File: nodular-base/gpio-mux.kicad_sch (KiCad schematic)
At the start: 6 parts, among them U24 AW9523B, U25 AW9523B, U26 AW9523B

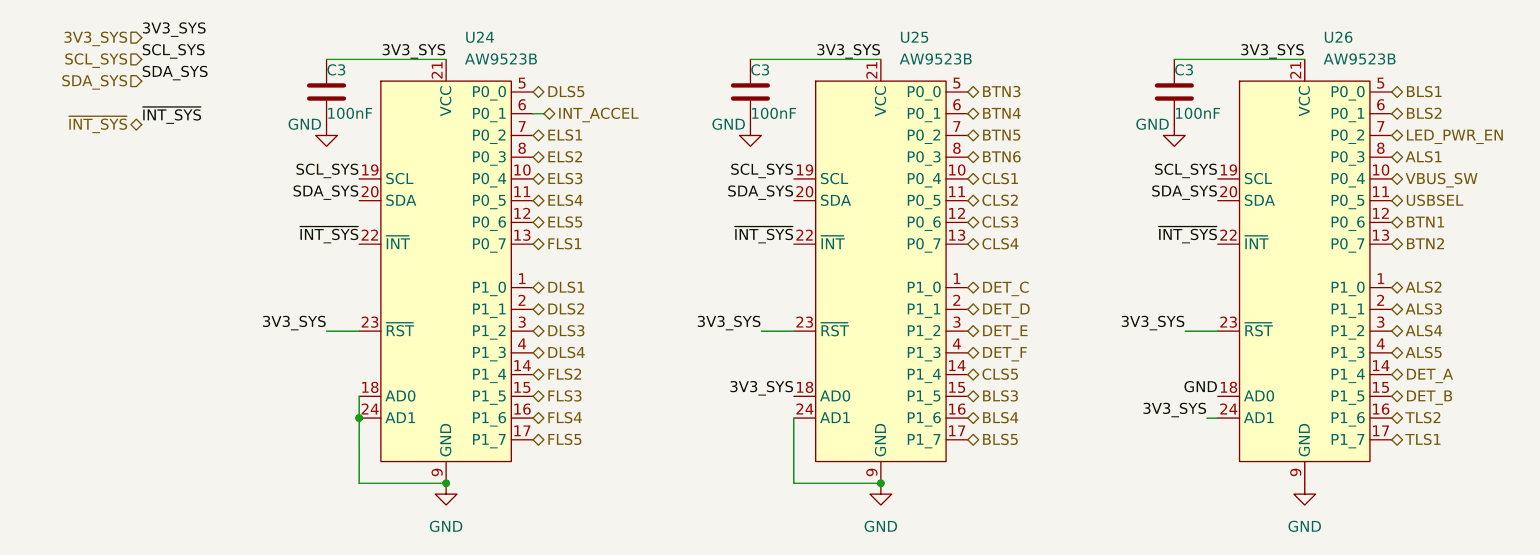
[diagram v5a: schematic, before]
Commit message: Modify base board: - Fix ESP32 strapping pins state - Remove 3/6 M3 standoffs - Change to LGA-style pads on ESP32 - Modify SFP mechanical pads to not be plated - Add larger mechanical pads with more solder paste surface to USB-C connectors
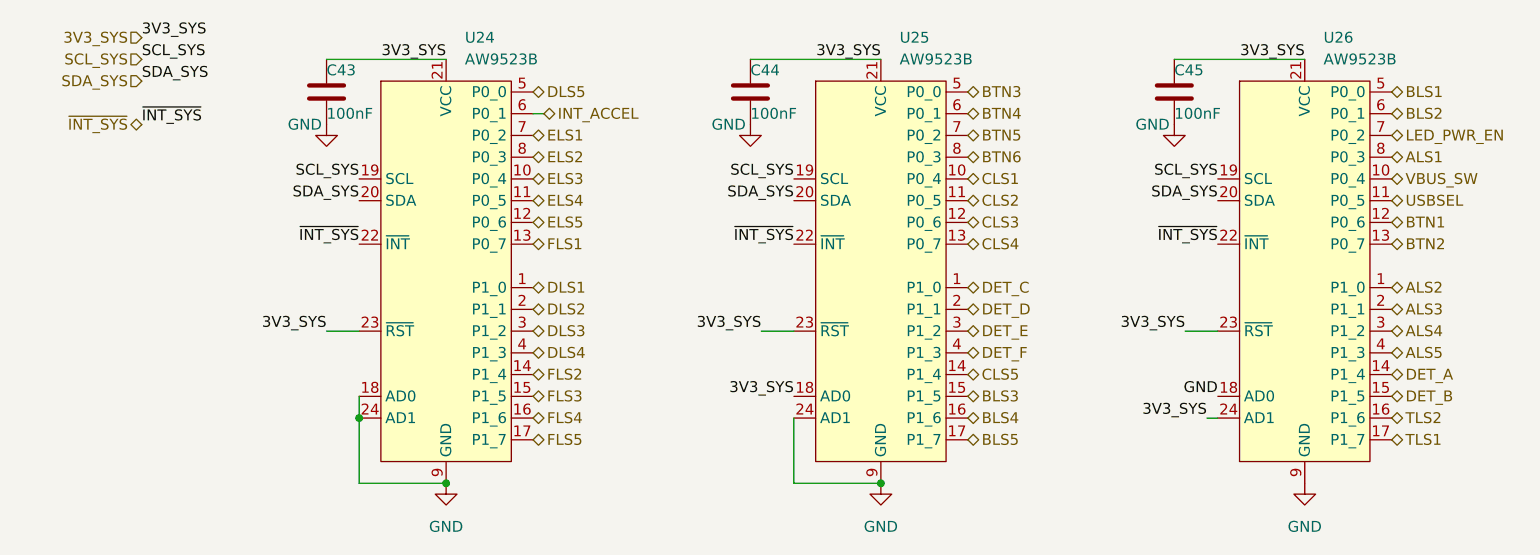
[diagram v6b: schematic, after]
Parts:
- renumbered C3 to C43, C3 to C44, C3 to C45
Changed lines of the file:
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@@
   (symbol (lib_id "Device:C") (at 180.34 64.77 0) (unit 1)
     (in_bom yes) (on_board yes) (dnp no)
-    (property "Reference" "C3" (at 180.34 62.23 0)
+    (property "Reference" "C45" (at 180.34 62.23 0)
       (effects (font (size 1.27 1.27)) (justify left))
     )
@@
     (instances
       (project "nodular-base"
-        (path "/6dcb0502-87e2-4c28-9ce8-81aab8925f06"
-          (reference "C3") (unit 1)
-        )
-        (path "/6dcb0502-87e2-4c28-9ce8-81aab8925f06/5ae693f9-48f3-406c-bbdf-b76d81cc71eb"
-          (reference "C16") (unit 1)
-        )
         (path "/6dcb0502-87e2-4c28-9ce8-81aab8925f06/52c49487-f3d5-40e2-8f19-e7b81498d838"
           (reference "C45") (unit 1)
@@
   (symbol (lib_id "Device:C") (at 130.81 64.77 0) (unit 1)
     (in_bom yes) (on_board yes) (dnp no)
-    (property "Reference" "C3" (at 130.81 62.23 0)
+    (property "Reference" "C44" (at 130.81 62.23 0)
       (effects (font (size 1.27 1.27)) (justify left))
     )
@@
     (instances
       (project "nodular-base"
-        (path "/6dcb0502-87e2-4c28-9ce8-81aab8925f06"
-          (reference "C3") (unit 1)
-        )
-        (path "/6dcb0502-87e2-4c28-9ce8-81aab8925f06/5ae693f9-48f3-406c-bbdf-b76d81cc71eb"
-          (reference "C16") (unit 1)
-        )
         (path "/6dcb0502-87e2-4c28-9ce8-81aab8925f06/52c49487-f3d5-40e2-8f19-e7b81498d838"
           (reference "C44") (unit 1)
@@
   (symbol (lib_id "Device:C") (at 81.28 64.77 0) (unit 1)
     (in_bom yes) (on_board yes) (dnp no)
-    (property "Reference" "C3" (at 81.28 62.23 0)
+    (property "Reference" "C43" (at 81.28 62.23 0)
       (effects (font (size 1.27 1.27)) (justify left))
     )
@@
     (instances
       (project "nodular-base"
-        (path "/6dcb0502-87e2-4c28-9ce8-81aab8925f06"
-          (reference "C3") (unit 1)
-        )
-        (path "/6dcb0502-87e2-4c28-9ce8-81aab8925f06/5ae693f9-48f3-406c-bbdf-b76d81cc71eb"
-          (reference "C16") (unit 1)
-        )
         (path "/6dcb0502-87e2-4c28-9ce8-81aab8925f06/52c49487-f3d5-40e2-8f19-e7b81498d838"
           (reference "C43") (unit 1)
